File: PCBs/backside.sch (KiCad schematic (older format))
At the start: 65 parts, among them J1 9Pin, J14 Conn_01x07_Male, J15 Conn_01x07_Male, J16 Conn_01x07_Male, J17 Conn_01x02_Male, J18 Conn_02x17_Odd_Even, J3 Power, J4 Conn_01x17_Male, J5 Matrix, J6 Conn_01x17_Male, J7 Driver output 2, J8 Conn_01x02_Male, J9 Conn_01x30_Male, Q1 IPP120P04P4L03, U1 HT1632C-52LQFP, U2 HT1632C-52LQFP, U3 STM32F103C8T6

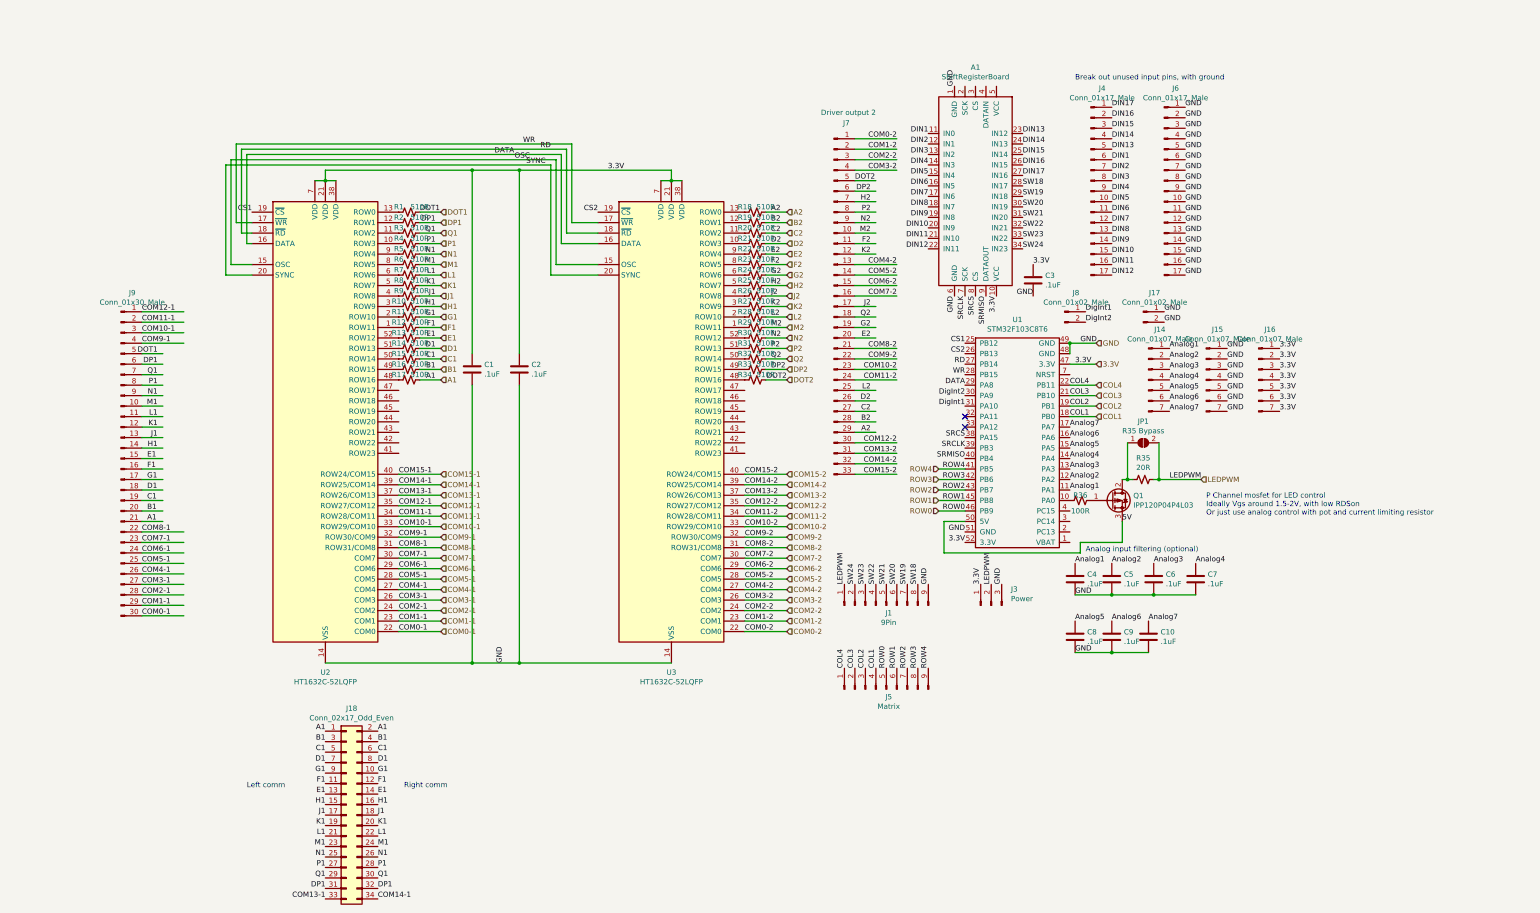
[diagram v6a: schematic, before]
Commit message: Major revision to backside PCB
Re-arranged pin assignments on the bluepill; sacrificed 4 Analog inputs for 2 more digital interrupts, and 2 more SPI CS pins.
Added two RJ12 connectors so that the board can be connected to other devices that use just shift registers, such as MFDs
Replaced footprint for 3x shift register sub-assembly PCB with 2 DIP16 74hc165s, and pullups and bypass caps.
Re-arranged and replaced 0.1" headers as appropriate.
Removed R35 and its bypass jumper, connecting LEDPWM directly to the MOSFET drain.
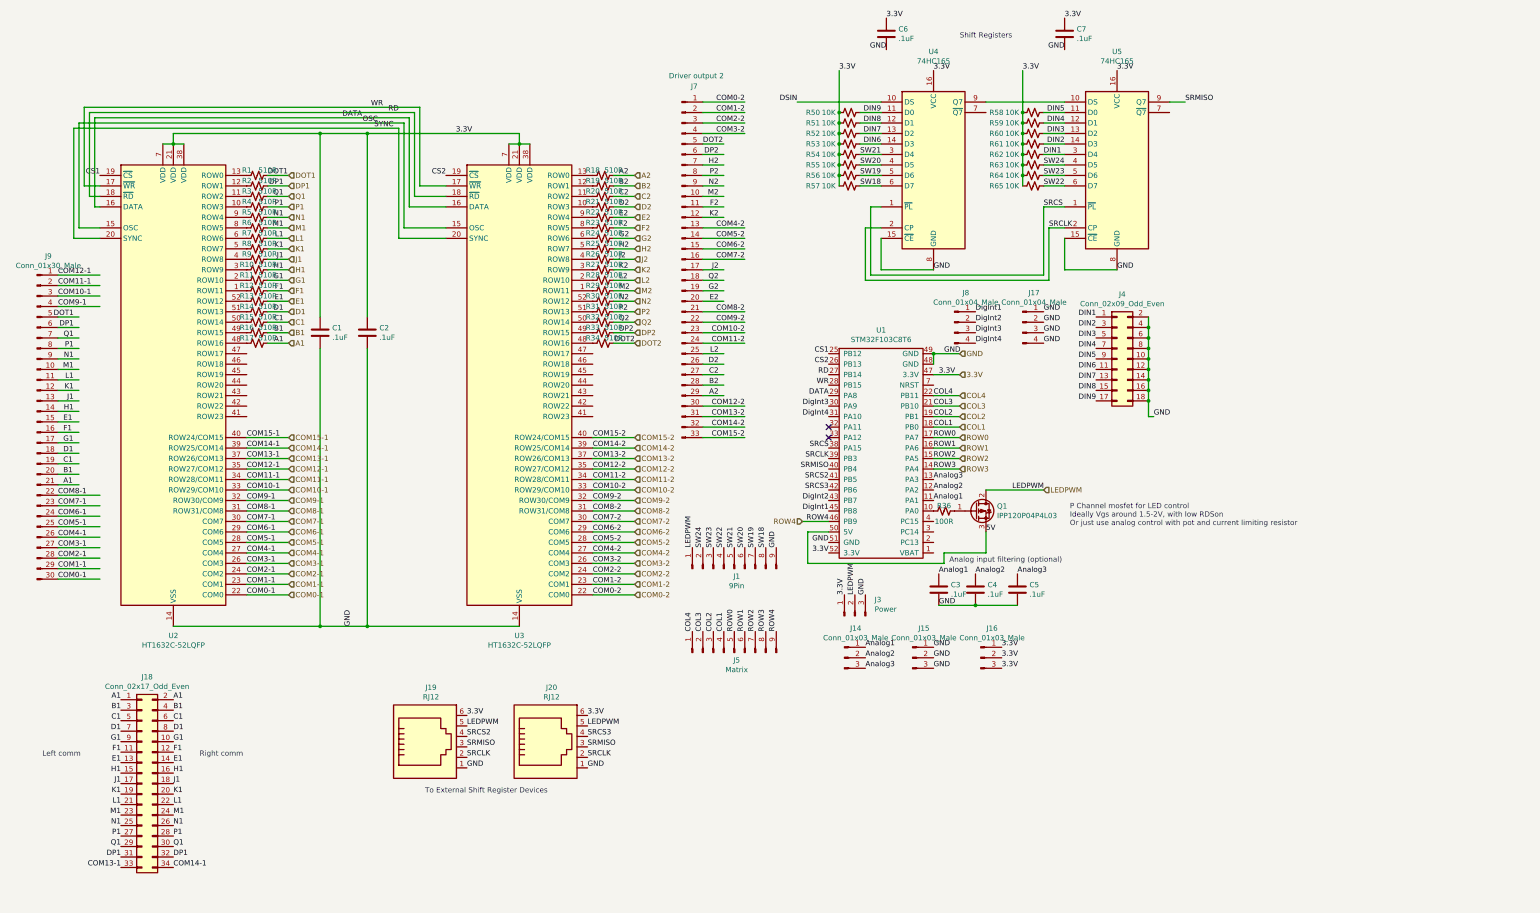
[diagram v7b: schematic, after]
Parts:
- removed A1: ShiftRegisterBoard, UFC:ShiftRegisterBoardPins, symbol UFClib:ShiftRegisterBoard
- removed C10, C8, C9: .1uF, Capacitor_SMD:C_0603_1608Metric_Pad1.08x0.95mm_HandSolder, symbol Device:C
- removed J14, J15, J16: Conn_01x07_Male, Connector_PinSocket_2.54mm:PinSocket_1x07_P2.54mm_Vertical, symbol Connector:Conn_01x07_Male
- removed J17, J8: Conn_01x02_Male, Connector_PinSocket_2.54mm:PinSocket_1x02_P2.54mm_Vertical, symbol Connector:Conn_01x02_Male
- removed J4, J6: Conn_01x17_Male, Connector_PinSocket_2.54mm:PinSocket_1x17_P2.54mm_Vertical, symbol Connector:Conn_01x17_Male
- removed JP1: R35 Bypass, Jumper:SolderJumper-2_P1.3mm_Open_Pad1.0x1.5mm, symbol Jumper:SolderJumper_2_Open
- removed R35: 20R, Resistor_SMD:R_1206_3216Metric_Pad1.30x1.75mm_HandSolder, symbol Device:R_Small_US
- added J14, J15, J16: Conn_01x03_Male, Connector_PinHeader_2.54mm:PinHeader_1x03_P2.54mm_Vertical, symbol Connector:Conn_01x03_Male
- added J17, J8: Conn_01x04_Male, Connector_PinHeader_2.54mm:PinHeader_1x04_P2.54mm_Vertical, symbol Connector:Conn_01x04_Male
- added J19, J20: RJ12, UFC:SS-6466-NF, symbol Connector:RJ12
- added J4: Conn_02x09_Odd_Even, Connector_PinHeader_2.54mm:PinHeader_2x09_P2.54mm_Vertical, symbol Connector_Generic:Conn_02x09_Odd_Even
- added R50, R51, R52, R53, R54, R55, R56, R57, R58, R59, R60, R61, R62, R63, R64, R65: 10K, Resistor_SMD:R_1206_3216Metric_Pad1.30x1.75mm_HandSolder, symbol Device:R_Small_US
- added U4, U5: 74HC165, Package_DIP:DIP-16_W7.62mm, symbol 74xx:74HC165
- renumbered C4 to C3, C5 to C4, C6 to C5, C3 to C6
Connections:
- net labels added: DSIN, DigInt3, DigInt4, SRCS2, SRCS3
- net labels removed: Analog4, Analog5, Analog6, Analog7, DIN10, DIN11, DIN12, DIN13, DIN14, DIN15, DIN16, DIN17
- wire segments 199 -> 250
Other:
- note added: "Shift Registers"
- note added: "To External Shift Register Devices"
- note removed: "Break out unused input pins, with ground"
- moved on the sheet: C1, C2, C3, C4, C5, C6, J1, J18, J3, J5, J7, J9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

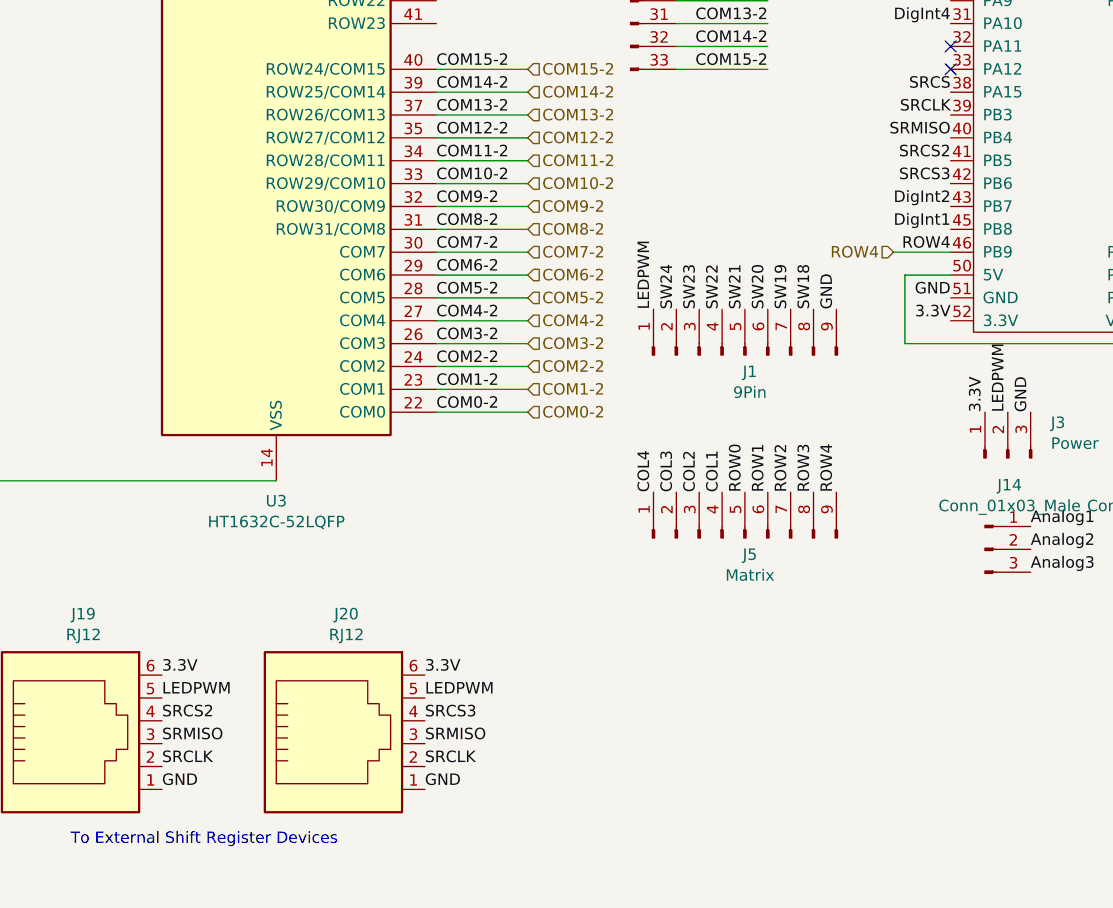
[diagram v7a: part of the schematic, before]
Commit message: Corrected extra shift register pins
Replaced two latch pins with one latch and one data to one port, and made the other port daisy chained after the two shift registers on the board
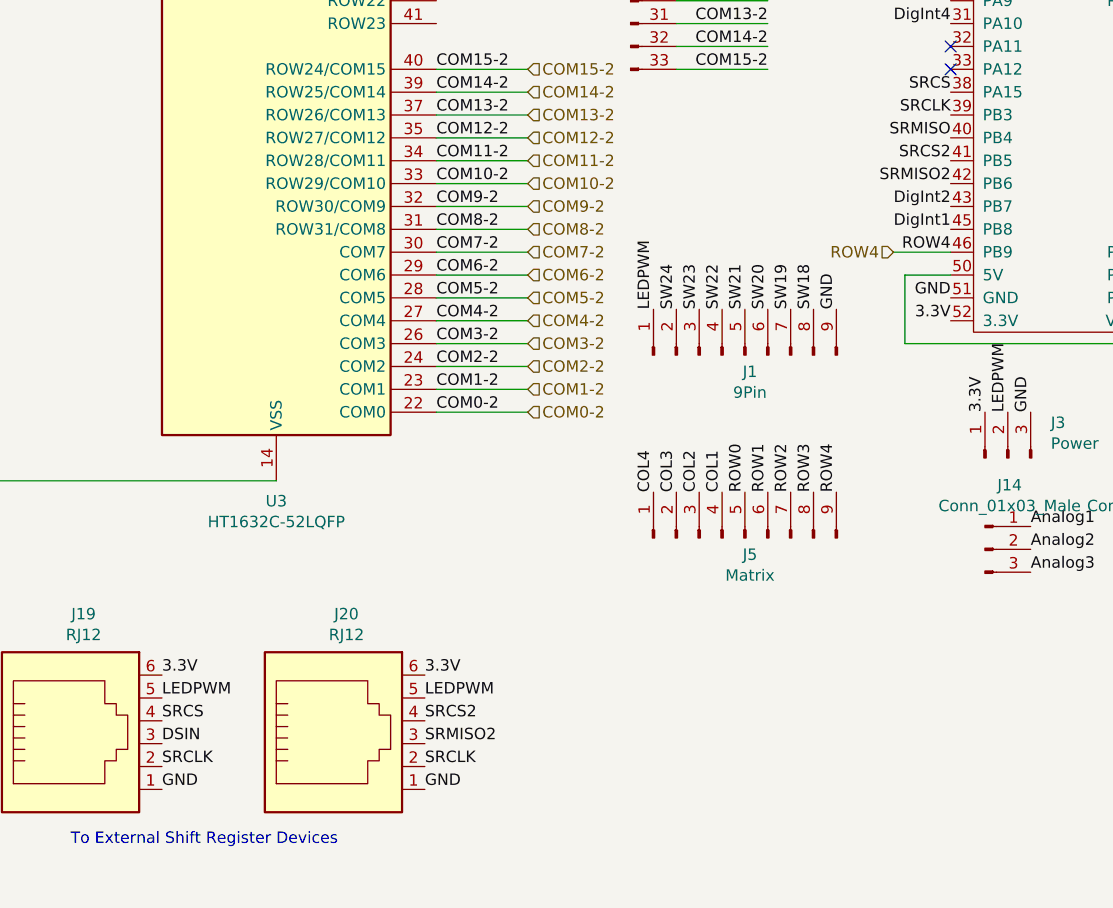
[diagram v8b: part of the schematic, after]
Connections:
- net labels added: SRMISO2
- net labels removed: SRCS3
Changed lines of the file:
@@
 $Descr A4 11693 8268
 encoding utf-8
-Sheet 1 1
+Sheet 3 3
 Title ""
 Date ""
@@
 SRCS2
 Text Label 7900 4600 2    50   ~ 0
-SRCS3
+SRMISO2
 Text Label 7900 3900 2    50   ~ 0
 DigInt4
@@
 LEDPWM
 Text Label 5600 6950 0    50   ~ 0
-SRCS3
+SRCS2
 Text Label 4450 6950 0    50   ~ 0
-SRCS2
+SRCS
 Text Label 4450 7050 0    50   ~ 0
-SRMISO
+DSIN
 Text Label 5600 7050 0    50   ~ 0
-SRMISO
+SRMISO2
 Text Label 5600 7150 0    50   ~ 0
 SRCLK
